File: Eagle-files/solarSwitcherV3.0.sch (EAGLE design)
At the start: 17 parts, among them T1 2N3440

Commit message: Started on version 3.0
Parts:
- added OK1: H11L1M, optocoupler:H11L1M
- R1: value 10k -> 100k
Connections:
- removed net N$10: C1.-, GREEN_LED.C, JP2.GND, JP4.4, SV2-2.S, T1.E, U$5.IN
- new net N$15: C1.-, D1.A, GREEN_LED.C, JP2.GND, JP3.GND, JP4.4, SV2-2.S, T1.E, U$2.COIL1, U$5.IN
- new net N$17: D1.C, OK1.OUT, U$2.COIL0
- net N$12: now also OK1.A, OK1.GND; no longer D1.C, U$2.COIL0
- net N$3: no longer D1.A, U$2.COIL1
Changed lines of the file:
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@@
 <parts>
 <part name="T1" library="transistor" deviceset="2N3440" device=""/>
-<part name="R1" library="resistor" deviceset="R-EU_" device="0207/10" value="10k"/>
+<part name="R1" library="resistor" deviceset="R-EU_" device="0207/10" value="100k"/>
 <part name="JP2" library="SparkFun-Connectors" deviceset="USB" device="PTH" value="USB-B"/>
 <part name="JP3" library="SparkFun-Connectors" deviceset="USB" device="PTH" value="USB-B"/>
@@
 <part name="R3" library="resistor" deviceset="R-EU_" device="0207/10" value="180"/>
 <part name="D2" library="diode" deviceset="1N4004" device=""/>
+<part name="OK1" library="optocoupler" deviceset="H11L*M" device="" technology="1"/>
 </parts>
 <sheets>
@@
 <instance part="R3" gate="G$1" x="132.08" y="-15.24" rot="R180"/>
 <instance part="D2" gate="1" x="127" y="38.1"/>
+<instance part="OK1" gate="G$1" x="160.02" y="-7.62" rot="R90"/>
 </instances>
 <busses>
@@
 <wire x1="17.78" y1="-15.24" x2="17.78" y2="-22.86" width="0.1524" layer="91"/>
 <junction x="17.78" y="-15.24"/>
-<pinref part="D1" gate="1" pin="A"/>
-<pinref part="U$2" gate="G$1" pin="COIL1"/>
-<wire x1="137.16" y1="-5.08" x2="144.78" y2="-5.08" width="0.1524" layer="91"/>
-<wire x1="144.78" y1="-5.08" x2="144.78" y2="-15.24" width="0.1524" layer="91"/>
 <pinref part="R3" gate="G$1" pin="1"/>
 <wire x1="144.78" y1="-15.24" x2="137.16" y2="-15.24" width="0.1524" layer="91"/>
-<wire x1="144.78" y1="-5.08" x2="144.78" y2="-2.54" width="0.1524" layer="91"/>
-<junction x="144.78" y="-5.08"/>
 <wire x1="17.78" y1="-22.86" x2="144.78" y2="-22.86" width="0.1524" layer="91"/>
 <wire x1="144.78" y1="-22.86" x2="144.78" y2="-15.24" width="0.1524" layer="91"/>
-<junction x="144.78" y="-15.24"/>
+<wire x1="165.1" y1="-15.24" x2="162.56" y2="-15.24" width="0.1524" layer="91"/>
+<wire x1="162.56" y1="-15.24" x2="162.56" y2="-22.86" width="0.1524" layer="91"/>
+<wire x1="162.56" y1="-22.86" x2="144.78" y2="-22.86" width="0.1524" layer="91"/>
+<junction x="144.78" y="-22.86"/>
 </segment>
 </net>
@@
 <wire x1="86.36" y1="2.54" x2="86.36" y2="5.08" width="0.1524" layer="91"/>
 <wire x1="86.36" y1="5.08" x2="86.36" y2="12.7" width="0.1524" layer="91"/>
-<wire x1="86.36" y1="12.7" x2="144.78" y2="12.7" width="0.1524" layer="91"/>
-<wire x1="144.78" y1="12.7" x2="144.78" y2="5.08" width="0.1524" layer="91"/>
-<pinref part="U$2" gate="G$1" pin="COIL0"/>
-<wire x1="144.78" y1="5.08" x2="137.16" y2="5.08" width="0.1524" layer="91"/>
-<pinref part="D1" gate="1" pin="C"/>
-<wire x1="144.78" y1="2.54" x2="144.78" y2="5.08" width="0.1524" layer="91"/>
-<junction x="144.78" y="5.08"/>
+<wire x1="86.36" y1="12.7" x2="162.56" y2="12.7" width="0.1524" layer="91"/>
 <wire x1="119.38" y1="5.08" x2="86.36" y2="5.08" width="0.1524" layer="91"/>
 <junction x="86.36" y="5.08"/>
+<pinref part="OK1" gate="G$1" pin="GND"/>
+<wire x1="162.56" y1="12.7" x2="162.56" y2="7.62" width="0.1524" layer="91"/>
+<wire x1="162.56" y1="7.62" x2="162.56" y2="2.54" width="0.1524" layer="91"/>
+<wire x1="162.56" y1="7.62" x2="172.72" y2="7.62" width="0.1524" layer="91"/>
+<wire x1="172.72" y1="7.62" x2="172.72" y2="-20.32" width="0.1524" layer="91"/>
+<junction x="162.56" y="7.62"/>
+<pinref part="OK1" gate="G$1" pin="A"/>
+<wire x1="172.72" y1="-20.32" x2="157.48" y2="-20.32" width="0.1524" layer="91"/>
+<wire x1="157.48" y1="-20.32" x2="157.48" y2="-17.78" width="0.1524" layer="91"/>
 </segment>
 </net>
@@
 </segment>
 </net>
-<net name="N$10" class="0">
-<segment>
+<net name="N$8" class="0">
+<segment>
+<pinref part="JP4" gate="G$1" pin="1"/>
+<pinref part="C1" gate="G$1" pin="+"/>
+<wire x1="137.16" y1="38.1" x2="152.4" y2="38.1" width="0.1524" layer="91"/>
+<pinref part="D2" gate="1" pin="C"/>
+<wire x1="129.54" y1="38.1" x2="137.16" y2="38.1" width="0.1524" layer="91"/>
+<junction x="137.16" y="38.1"/>
+</segment>
+</net>
+<net name="N$17" class="0">
+<segment>
+<pinref part="U$2" gate="G$1" pin="COIL0"/>
+<pinref part="D1" gate="1" pin="C"/>
+<wire x1="144.78" y1="2.54" x2="144.78" y2="5.08" width="0.1524" layer="91"/>
+<junction x="144.78" y="5.08"/>
+<pinref part="OK1" gate="G$1" pin="OUT"/>
+<wire x1="160.02" y1="2.54" x2="160.02" y2="5.08" width="0.1524" layer="91"/>
+<wire x1="160.02" y1="5.08" x2="144.78" y2="5.08" width="0.1524" layer="91"/>
+<wire x1="144.78" y1="5.08" x2="137.16" y2="5.08" width="0.1524" layer="91"/>
+</segment>
+</net>
+<net name="N$15" class="0">
+<segment>
+<pinref part="D1" gate="1" pin="A"/>
+<wire x1="144.78" y1="-5.08" x2="144.78" y2="-2.54" width="0.1524" layer="91"/>
+<pinref part="U$2" gate="G$1" pin="COIL1"/>
+<wire x1="137.16" y1="-5.08" x2="144.78" y2="-5.08" width="0.1524" layer="91"/>
+<wire x1="144.78" y1="-5.08" x2="144.78" y2="-10.16" width="0.1524" layer="91"/>
+<junction x="144.78" y="-5.08"/>
 <pinref part="JP4" gate="G$1" pin="4"/>
 <pinref part="C1" gate="G$1" pin="-"/>
@@
 <junction x="83.82" y="30.48"/>
 <pinref part="GREEN_LED" gate="G$1" pin="C"/>
-<wire x1="83.82" y1="30.48" x2="12.7" y2="30.48" width="0.1524" layer="91"/>
+<wire x1="83.82" y1="30.48" x2="53.34" y2="30.48" width="0.1524" layer="91"/>
+<wire x1="53.34" y1="30.48" x2="30.48" y2="30.48" width="0.1524" layer="91"/>
+<wire x1="30.48" y1="30.48" x2="12.7" y2="30.48" width="0.1524" layer="91"/>
 <wire x1="12.7" y1="30.48" x2="12.7" y2="40.64" width="0.1524" layer="91"/>
 <wire x1="12.7" y1="30.48" x2="-43.18" y2="30.48" width="0.1524" layer="91"/>
@@
 <wire x1="137.16" y1="30.48" x2="83.82" y2="30.48" width="0.1524" layer="91"/>
 <junction x="137.16" y="30.48"/>
-</segment>
-</net>
-<net name="N$8" class="0">
-<segment>
-<pinref part="JP4" gate="G$1" pin="1"/>
-<pinref part="C1" gate="G$1" pin="+"/>
-<wire x1="137.16" y1="38.1" x2="152.4" y2="38.1" width="0.1524" layer="91"/>
-<pinref part="D2" gate="1" pin="C"/>
-<wire x1="129.54" y1="38.1" x2="137.16" y2="38.1" width="0.1524" layer="91"/>
-<junction x="137.16" y="38.1"/>
-</segment>
-</net>
+<pinref part="JP3" gate="G$1" pin="GND"/>
+<wire x1="53.34" y1="2.54" x2="53.34" y2="30.48" width="0.1524" layer="91"/>
+<junction x="53.34" y="30.48"/>
+<wire x1="144.78" y1="-10.16" x2="30.48" y2="-10.16" width="0.1524" layer="91"/>
+<wire x1="30.48" y1="-10.16" x2="30.48" y2="30.48" width="0.1524" layer="91"/>
+<junction x="30.48" y="30.48"/>
+</segment>
+</net>

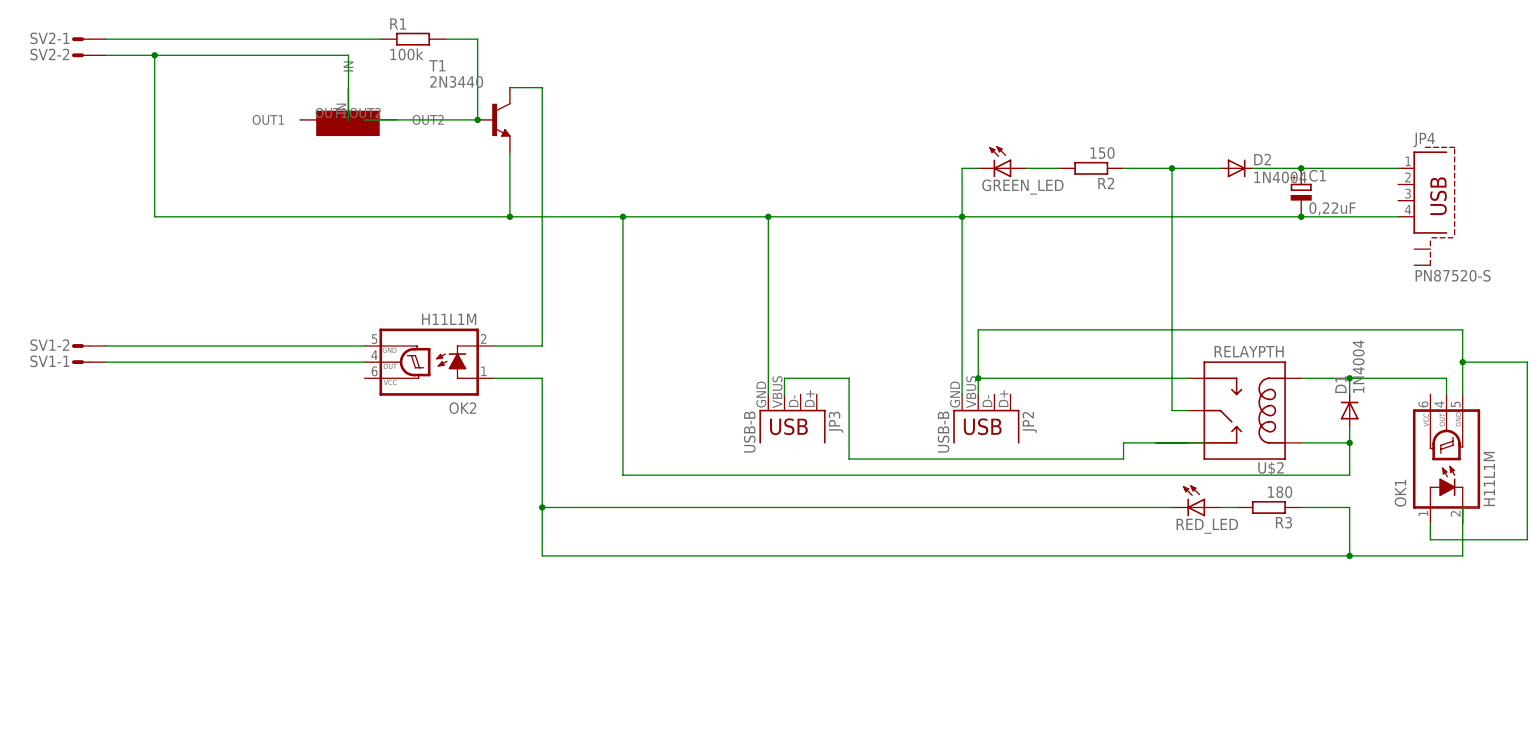
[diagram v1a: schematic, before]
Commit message: Placed and connected all components
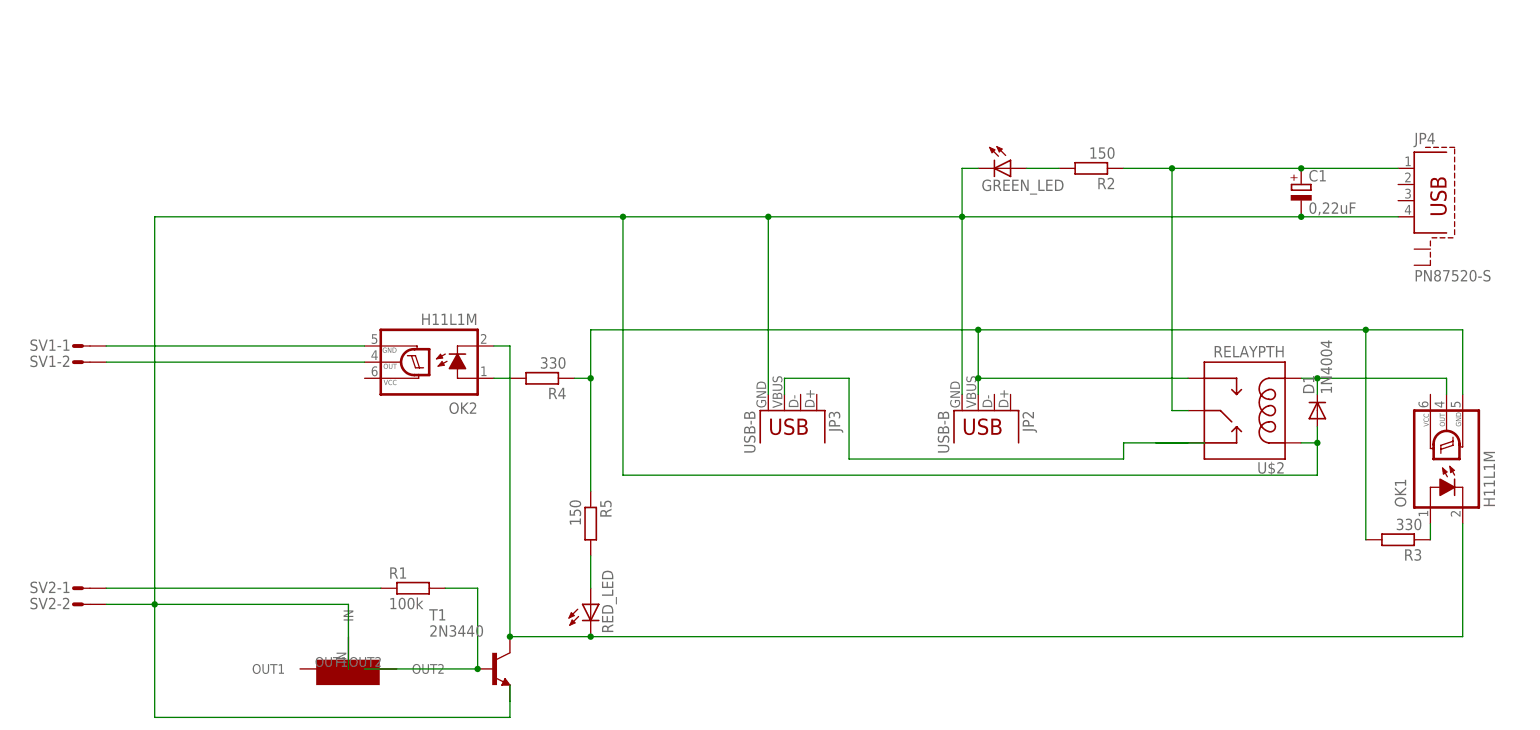
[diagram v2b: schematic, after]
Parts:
- removed D2: 1N4004, diode:1N4004
- added R4: 330, resistor:R-EU_0207/10
- added R5: 150, resistor:R-EU_0207/10
- R3: value 180 -> 330
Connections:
- removed net N$2: D2.A, R2.1, U$2.SWCOMMON
- new net N$18: OK1.A, R3.1
- net N$12: now also R3.2, R4.1, R5.1; no longer OK1.A
- net N$14: now also R5.2; no longer R3.2
- net N$3: now also R4.2; no longer R3.1, RED_LED.C
- net N$4: now also SV1-2.S; no longer SV1-1.S
- net N$7: now also SV1-1.S; no longer SV1-2.S
- net N$8: now also R2.1, U$2.SWCOMMON; no longer D2.C
- net N$9: now also OK1.C, RED_LED.C
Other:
- moved on the sheet: D1, R1, R3, RED_LED, SV1-1, SV1-2, SV2-1, SV2-2, T1
